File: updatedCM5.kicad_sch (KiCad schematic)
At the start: 12 parts, among them J11 USB_C_Receptacle_USB2.0

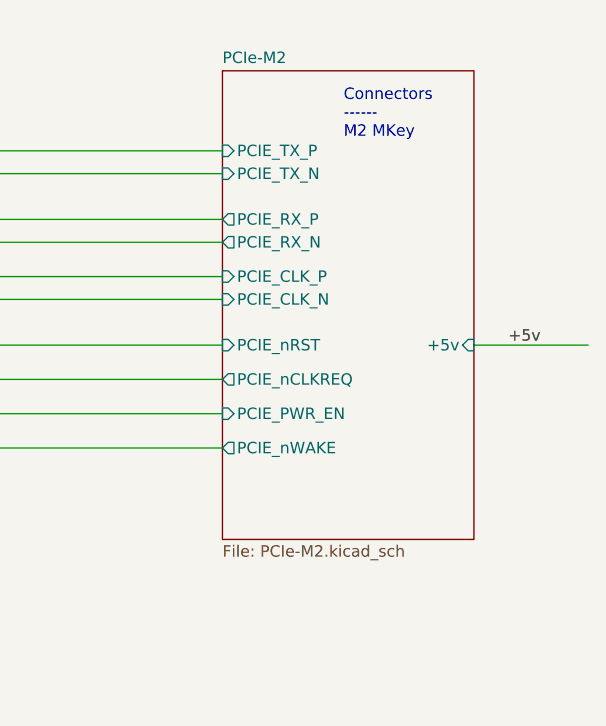
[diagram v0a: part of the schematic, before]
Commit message: Removed ERC errors and M2 connector
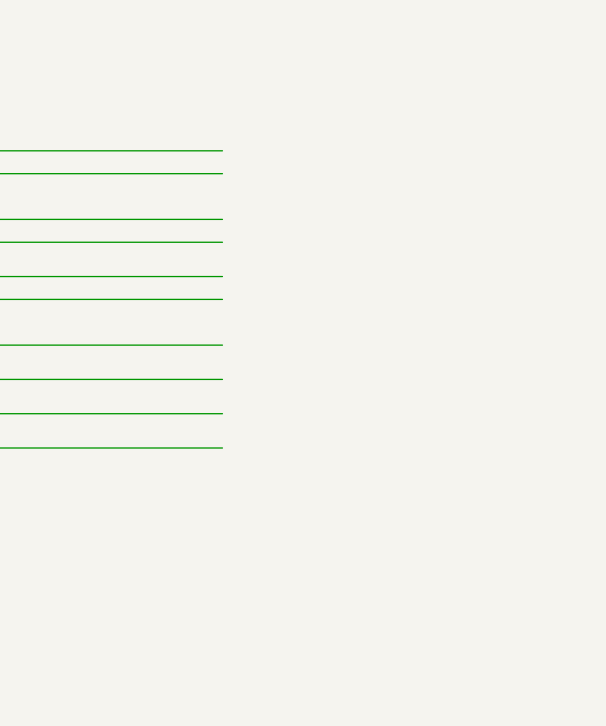
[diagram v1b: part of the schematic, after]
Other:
- removed sheet PCIe-M2
- note removed: "Connectors ------ M2 MKey"
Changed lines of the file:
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@@
-		)
-	)
-	(text "Connectors\n------\nM2 MKey"
-		(exclude_from_sim no)
-		(at 228.092 41.91 0)
-		(effects
-			(font
-				(size 1.27 1.27)
-			)
-			(justify left bottom)
 		)
 	)
@@
 	(wire
 		(pts
-			(xy 242.57 64.77) (xy 255.27 64.77)
-		)
-		(stroke
-			(width 0)
-			(type solid)
-		)
-	)
-	(wire
-		(pts
 			(xy 186.69 72.39) (xy 214.63 72.39)
 		)
@@
 	(label "CC2"
 		(at 119.38 133.35 0)
-		(effects
-			(font
-				(size 1.27 1.27)
-			)
-			(justify left bottom)
-		)
-	)
-	(label "+5v"
-		(at 246.38 64.77 0)
 		(effects
 			(font
@@
 				)
 			)
-		)
-	)
-	(sheet
-		(at 214.63 34.29)
-		(size 27.94 52.07)
-		(exclude_from_sim no)
-		(in_bom yes)
-		(on_board yes)
-		(dnp no)
-		(fields_autoplaced yes)
-		(stroke
-			(width 0.152)
-			(type solid)
-			(color 132 0 132 1)
-		)
-		(fill
-			(color 255 255 255 0.0000)
-		)
-		(property "Sheetname" "PCIe-M2"
-			(at 214.63 33.5786 0)
-			(effects
-				(font
-					(size 1.27 1.27)
-				)
-				(justify left bottom)
-			)
-		)
-		(property "Sheetfile" "PCIe-M2.kicad_sch"
-			(at 214.63 86.9444 0)
-			(effects
-				(font
-					(size 1.27 1.27)
-				)
-				(justify left top)
-			)
-		)
-		(pin "PCIE_CLK_P" input
-			(at 214.63 57.15 180)
-			(effects
-				(font
-					(size 1.27 1.27)
-				)
-				(justify left)
-			)
-		)
-		(pin "PCIE_CLK_N" input
-			(at 214.63 59.69 180)
-			(effects
-				(font
-					(size 1.27 1.27)
-				)
-				(justify left)
-			)
-		)
-		(pin "PCIE_TX_P" input
-			(at 214.63 43.18 180)
-			(effects
-				(font
-					(size 1.27 1.27)
-				)
-				(justify left)
-			)
-		)
-		(pin "PCIE_TX_N" input
-			(at 214.63 45.72 180)
-			(effects
-				(font
-					(size 1.27 1.27)
-				)
-				(justify left)
-			)
-		)
-		(pin "PCIE_nCLKREQ" output
-			(at 214.63 68.58 180)
-			(effects
-				(font
-					(size 1.27 1.27)
-				)
-				(justify left)
-			)
-		)
-		(pin "PCIE_nRST" input
-			(at 214.63 64.77 180)
-			(effects
-				(font
-					(size 1.27 1.27)
-				)
-				(justify left)
-			)
-		)
-		(pin "PCIE_RX_P" output
-			(at 214.63 50.8 180)
-			(effects
-				(font
-					(size 1.27 1.27)
-				)
-				(justify left)
-			)
-		)
-		(pin "PCIE_RX_N" output
-			(at 214.63 53.34 180)
-			(effects
-				(font
-					(size 1.27 1.27)
-				)
-				(justify left)
-			)
-		)
-		(pin "+5v" input
-			(at 242.57 64.77 0)
-			(effects
-				(font
-					(size 1.27 1.27)
-				)
-				(justify right)
-			)
-		)
-		(pin "PCIE_PWR_EN" input
-			(at 214.63 72.39 180)
-			(effects
-				(font
-					(size 1.27 1.27)
-				)
-				(justify left)
-			)
-		)
-		(pin "PCIE_nWAKE" output
-			(at 214.63 76.2 180)
-			(effects
-				(font
-					(size 1.27 1.27)
-				)
-				(justify left)
-			)
-		)
-		(instances
-			(project "updatedCM5"
-				(path "/e63e39d7-6ac0-4ffd-8aa3-1841a4541b55"
-					(page "4")
-				)
-			)
